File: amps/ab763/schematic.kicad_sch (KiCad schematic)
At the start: 115 parts, among them T1 125P33A, T2 125C3A, T3 125A1A, T4 125A20B

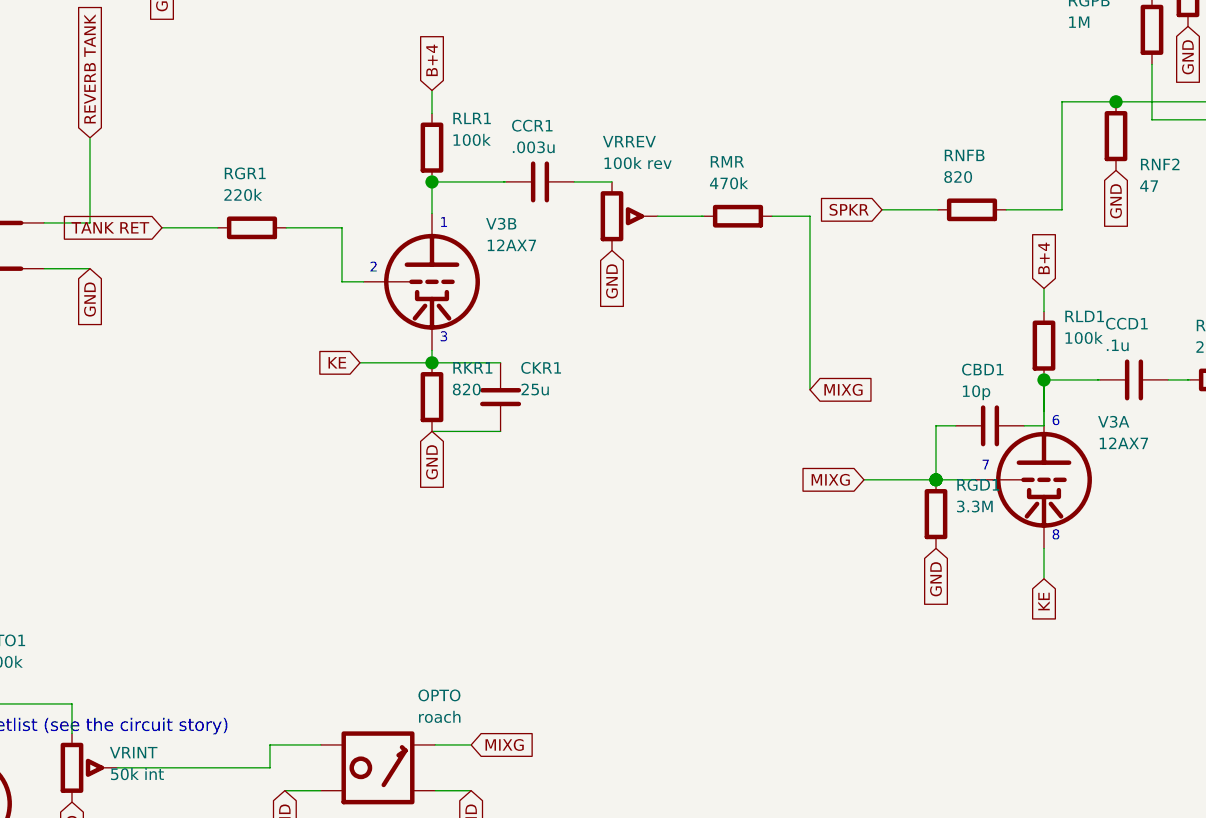
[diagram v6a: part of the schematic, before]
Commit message: Fix: the AB763 mix driver's grid leak was a 3.3M the drawing puts in series, and the reverb return a 220k it puts to ground
The C-FD schematic, read at native size, is VERIFIED on netlist and sheet.
DC operating points are unchanged: GD1 and GR1 sit at 0 V either way, and
verify_amps passes with op-points.yaml as committed.

- Mix-driver grid (node GD1). The drawing's return to ground is a 220k
  (RGD2, new in the parts list, absent until now). The 3.3M (RGD1) with
  its 10 pF (CBD1) sits in SERIES, from the far side of the vibrato
  channel's .02 coupler to the grid, beside the 470k from the Reverb wiper.
  The netlist modelled the 3.3M as the grid leak. The sheet drew it to
  ground, and drew CBD1 from the grid to the plate. Netlist: RGD1 GD1 0
  3.3meg -> RGD2 GD1 0 220k. Sheet: RGD1 || CBD1 from the RVSEND net (the
  .02's far side, which also feeds the reverb send) to the grid; RGD2 from
  the grid to GND.
- Reverb-recovery grid (node GR1). The drawing puts the tank-return plug, a
  220k to ground and the reverb-pedal switch all on the grid node. The layout
  mounts the 220k at the reverb-pedal jack and wires that jack to the
  tank-return jack. The sheet drew RGR1 in SERIES between the tank and the
  grid, and the netlist stood a 1M (RGRV) in for the return. Netlist: RGRV
  GR1 0 1meg -> RGR1 GR1 0 220k. Sheet: TANK RET on the grid, RGR1 from
  the grid to GND.
- bom.yaml: RGD2 added. RGD1, CBD1, RGR1, CCV2 and CRS roles say what
  each part joins.

verify_schematic_nets ab763: PASS (claimed). The board follows in the next
commit.

Co-Authored-By: Claude Opus 5 (1M context) <noreply@anthropic.com>
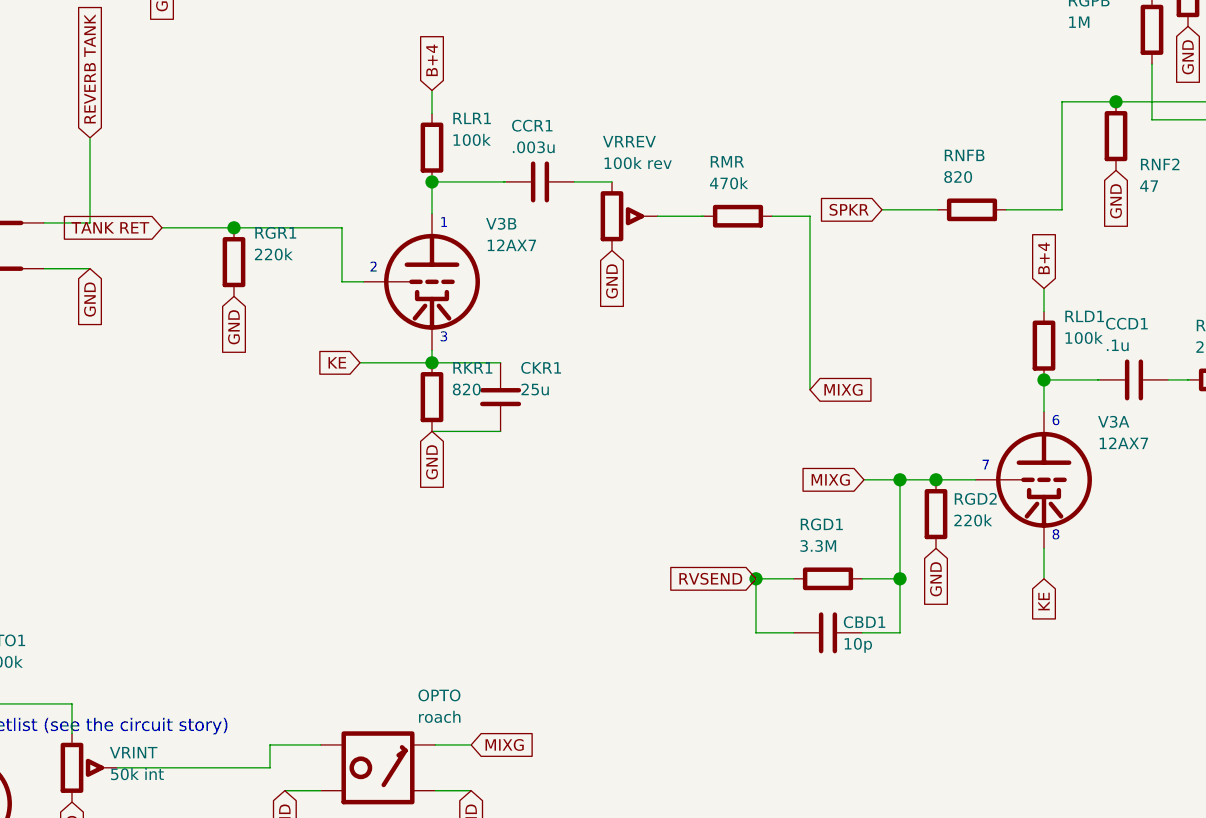
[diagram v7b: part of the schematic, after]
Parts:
- removed CCD1: .1u, symbol cx:C
- removed RD1: 10k, symbol cx:R
- removed RGD1: 3.3M, symbol cx:R
- removed RGL1, RMD1: 220k, symbol cx:R
- removed RT2: 22k, symbol cx:R
- removed RTOG3: 1M, symbol cx:R
- removed V5B: 12AX7, symbol cx:TRIODE
- added C13: 16u, symbol cx:C
- added RGD2: 220k, symbol cx:R
- added RGPB: 1M, symbol cx:R
- added RKTO1: 2.7k, symbol cx:R
- added RTO10: 10M, symbol cx:R
- added V3A, V5A: 12AX7, symbol cx:TRIODE
- added V8: 6V6GT, symbol cx:PENTODE
- added VRSPD: 3M speed, symbol cx:POT
- CCD1: renamed from V5A; value 12AX7 -> .1u; symbol cx:TRIODE -> cx:C
- RD1: renamed from C12; value 16u -> 10k; symbol cx:C -> cx:R
- RGD1: renamed from V3A; value 12AX7 -> 3.3M; symbol cx:TRIODE -> cx:R
- RGL1: renamed from V8; value 6V6GT -> 220k; symbol cx:PENTODE -> cx:R
- RKTO2: renamed from RTO10; value 10M -> 100k
- RT2: renamed from RGPB; value 1M -> 22k
- RTO2: renamed from RKTO2; value 100k -> 220k
- RTOG3: renamed from VRSPD; value 3M speed -> 1M; symbol cx:POT -> cx:R
- V5B: renamed from RKTO1; value 2.7k -> 12AX7; symbol cx:R -> cx:TRIODE
- renumbered C13 to C12, RTO2 to RMD1
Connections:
- net -35V: now also RGL1.2
- net B+2: now also RD1.1
- net B+3: now also C12.1, RD1.2; no longer RD1.1
- net B+4: now also RTO2.1, C13.1; no longer C12.1, RMD1.1
- net GND: now also RGR1.2, RT2.2, RTOG3.2, C13.2, RGD2.2, RKTO1.2, RTO10.2, V8.4 (K), VRSPD.3; no longer RD1.2, RGL1.4 (K), RTO2.2, RTOG3.3, V5B.2
- net KE: now also V3A.3 (K); no longer RGD1.3 (K)
- net MIXG: now also CBD1.2, RGD2.1, V3A.2 (G); no longer CBD1.1
- net PIG: now also RMD1.2
- net RVSEND: now also CBD1.1, RGD1.1
- net TANK RET: now also V3B.2 (G)
- net at RKTO2.1: now also V5B.3 (K); no longer CTO3.2
- net at CPIB.2, V6B.2 (G): now also RGPB.2; no longer RT2.2
- net at C1.2, V7.2 (G1): now also RGL1.1
- net at V5B.1 (P): now also RTO1.2, VRINT.1; no longer CCD1.3 (K)
- net at T3.3 (PRI_B): now also V8.1 (P); no longer RGL1.1 (P)
- net at C2.2, RGL2.1: now also V8.2 (G1); no longer RGL1.2 (G1)
- net at RGPA.2, RT2.1, RTAIL.1: now also RGPB.1
- net at RS2.1: now also V8.3 (G2); no longer RGL1.3 (G2)
- net at CTO2.1, RTOG.1, RTOG3.1: now also V5A.2 (G), VRSPD.1, VRSPD.2 (W); no longer CCD1.2 (G), RTOG3.2 (W)
- net at CTO1.2, CTO3.1: now also RTO2.2, V5A.1 (P); no longer CCD1.1 (P), RMD1.2
- new net: CTO3.2, RTO10.1, V5B.2 (G)
- new net: RKTO1.1, V5A.3 (K)
- new net: CCD1.1, RLD1.2, V3A.1 (P)
- new net: CCD1.2, RMD1.1
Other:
- moved on the sheet: C12, RKTO2, RMD1, RT2, RTO2
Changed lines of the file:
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@@
   (global_label "TANK RET" (shape input) (at 127.7 122.278 180)
     (effects (font (size 1.27 1.27)) (justify right)))
-  (symbol (lib_id "cx:R") (at 137.7 122.278 90) (unit 1)
+  (wire (pts (xy 127.7 122.278) (xy 135.7 122.278))
+    (stroke (width 0) (type default)))
+  (wire (pts (xy 135.7 122.278) (xy 147.7 122.278))
+    (stroke (width 0) (type default)))
+  (junction (at 135.7 122.278) (diameter 1.467) (color 0 0 0 0))
+  (symbol (lib_id "cx:R") (at 135.7 126.088 0) (unit 1)
     (in_bom yes) (on_board yes)
-    (property "Reference" "RGR1" (at 134.5 116.278 270) (effects (font (size 1.27 1.27)) (justify left)))
-    (property "Value" "220k" (at 134.5 118.678 270) (effects (font (size 1.27 1.27)) (justify left))))
-  (wire (pts (xy 127.7 122.278) (xy 133.89 122.278))
-    (stroke (width 0) (type default)))
-  (wire (pts (xy 141.51 122.278) (xy 147.7 122.278))
-    (stroke (width 0) (type default)))
+    (property "Reference" "RGR1" (at 137.9 122.888 0) (effects (font (size 1.27 1.27)) (justify left)))
+    (property "Value" "220k" (at 137.9 125.288 0) (effects (font (size 1.27 1.27)) (justify left))))
+  (global_label "GND" (shape input) (at 135.7 129.898 270)
+    (effects (font (size 1.27 1.27)) (justify right)))
   (wire (pts (xy 147.7 122.278) (xy 147.7 128.278))
     (stroke (width 0) (type default)))
@@
   (global_label "MIXG" (shape input) (at 205.7 150.278 180)
     (effects (font (size 1.27 1.27)) (justify right)))
-  (wire (pts (xy 205.7 150.278) (xy 213.7 150.278))
+  (wire (pts (xy 205.7 150.278) (xy 209.7 150.278))
     (stroke (width 0) (type default)))
+  (wire (pts (xy 209.7 150.278) (xy 213.7 150.278))
+    (stroke (width 0) (type default)))
+  (junction (at 209.7 150.278) (diameter 1.467) (color 0 0 0 0))
   (junction (at 213.7 150.278) (diameter 1.467) (color 0 0 0 0))
   (symbol (lib_id "cx:R") (at 213.7 154.088 0) (unit 1)
     (in_bom yes) (on_board yes)
-    (property "Reference" "RGD1" (at 215.9 150.888 0) (effects (font (size 1.27 1.27)) (justify left)))
-    (property "Value" "3.3M" (at 215.9 153.288 0) (effects (font (size 1.27 1.27)) (justify left))))
+    (property "Reference" "RGD2" (at 215.616 152.448 0) (effects (font (size 1.27 1.27)) (justify left)))
+    (property "Value" "220k" (at 215.616 154.848 0) (effects (font (size 1.27 1.27)) (justify left))))
   (global_label "GND" (shape input) (at 213.7 157.898 270)
     (effects (font (size 1.27 1.27)) (justify right)))
-  (wire (pts (xy 213.7 150.278) (xy 213.7 144.278))
+  (wire (pts (xy 209.7 150.278) (xy 209.7 161.278))
     (stroke (width 0) (type default)))
-  (symbol (lib_id "cx:C") (at 219.7 144.278 90) (unit 1)
+  (wire (pts (xy 209.7 161.278) (xy 209.7 167.278))
+    (stroke (width 0) (type default)))
+  (symbol (lib_id "cx:R") (at 201.7 161.278 90) (unit 1)
     (in_bom yes) (on_board yes)
-    (property "Reference" "CBD1" (at 216.5 138.078 270) (effects (font (size 1.27 1.27)) (justify left)))
-    (property "Value" "10p" (at 216.5 140.478 270) (effects (font (size 1.27 1.27)) (justify left))))
-  (wire (pts (xy 213.7 144.278) (xy 215.89 144.278))
+    (property "Reference" "RGD1" (at 198.5 155.278 270) (effects (font (size 1.27 1.27)) (justify left)))
+    (property "Value" "3.3M" (at 198.5 157.678 270) (effects (font (size 1.27 1.27)) (justify left))))
+  (wire (pts (xy 209.7 161.278) (xy 205.51 161.278))
     (stroke (width 0) (type default)))
-  (wire (pts (xy 223.51 144.278) (xy 225.7 144.278))
+  (wire (pts (xy 197.89 161.278) (xy 193.7 161.278))
     (stroke (width 0) (type default)))
-  (wire (pts (xy 225.7 144.278) (xy 225.7 142.658))
+  (symbol (lib_id "cx:C") (at 201.7 167.278 90) (unit 1)
+    (in_bom yes) (on_board yes)
+    (property "Reference" "CBD1" (at 203.362 166.146 270) (effects (font (size 1.27 1.27)) (justify left)))
+    (property "Value" "10p" (at 203.362 168.546 270) (effects (font (size 1.27 1.27)) (justify left))))
+  (wire (pts (xy 209.7 167.278) (xy 205.51 167.278))
     (stroke (width 0) (type default)))
-  (wire (pts (xy 225.7 142.658) (xy 225.7 139.178))
+  (wire (pts (xy 197.89 167.278) (xy 193.7 167.278))
     (stroke (width 0) (type default)))
+  (wire (pts (xy 193.7 161.278) (xy 193.7 167.278))
+    (stroke (width 0) (type default)))
+  (junction (at 193.7 161.278) (diameter 1.467) (color 0 0 0 0))
+  (junction (at 209.7 161.278) (diameter 1.467) (color 0 0 0 0))
+  (global_label "RVSEND" (shape input) (at 193.7 161.278 180)
+    (effects (font (size 1.27 1.27)) (justify right)))
   (symbol (lib_id "cx:TRIODE") (at 225.7 150.278 0) (unit 1)
     (in_bom yes) (on_board yes)
@@
   (wire (pts (xy 213.7 150.278) (xy 218.08 150.278))
     (stroke (width 0) (type default)))
-  (junction (at 213.7 150.278) (diameter 1.467) (color 0 0 0 0))
   (wire (pts (xy 225.7 142.658) (xy 225.7 139.178))
     (stroke (width 0) (type default)))

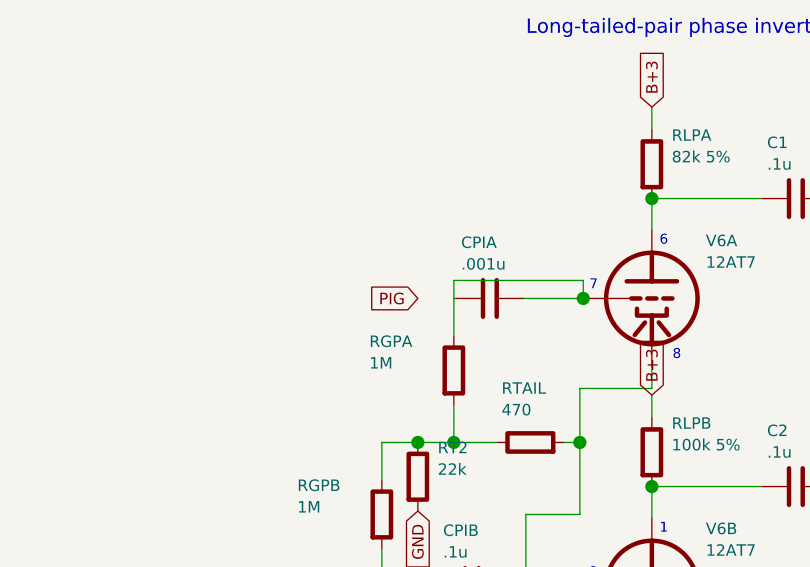
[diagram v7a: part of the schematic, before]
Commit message: Fix: the AB763 sheet's mix node never reached the phase inverter; its .001 coupler sat with both ends on the hot grid
The sheet placed the PI-side PIG label at x=232, but started the lead into
CPIA at x=236, so the label touched nothing. CPIA's left pin also landed on
the RGPA riser (x=236, y=98–104) with a T-tap. The 0.001 µF coupler therefore
sat with both ends on V6A's grid net. The mix node (both channels' 220k
mixing resistors) reached the inverter on no net at all. Neither half is in
the DC netlist, so the sheet↔netlist gate could not see it. It surfaced when
the board placed CPIA as the C-FD layout does, and sheet↔board reported
"the sheet shorts its two ends onto one net".

CPIA now sits left of the RGPA riser, and its lead starts at the label.
CPIA.1 is on {PIG, RMN2, RMD1}; CPIA.2 is on {RGPA, V6A grid}; the riser
crosses the coupler's lead without joining it. A per-anchor scan (every label
anchor must touch a wire, a pin or a junction) now finds none dangling on
this sheet. It finds one MIXG anchor dangling on each of the Super Reverb
and Twin Reverb sheets, which belong to #35.

Co-Authored-By: Claude Opus 5 (1M context) <noreply@anthropic.com>
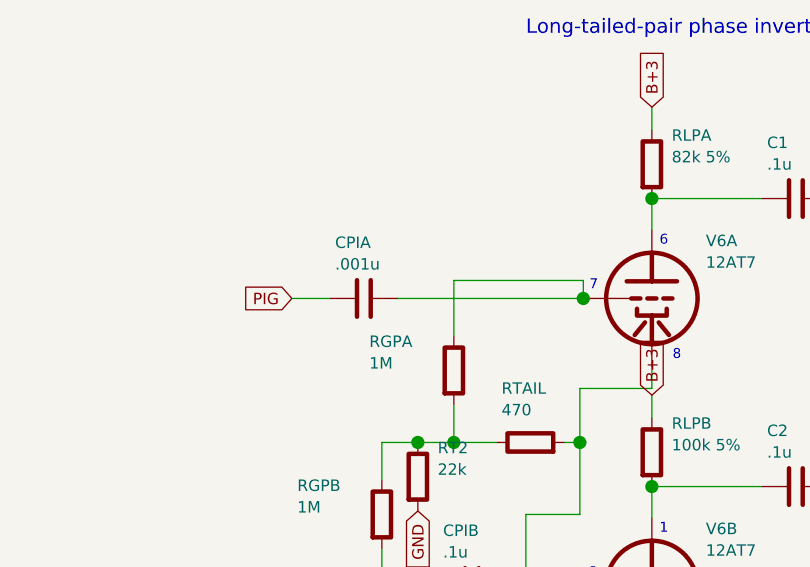
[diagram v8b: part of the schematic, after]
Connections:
- net PIG: now also CPIA.1
- net at CPIA.2, RGPA.1, V6A.2 (G): no longer CPIA.1
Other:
- moved on the sheet: CPIA
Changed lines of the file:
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@@
   (text "Long-tailed-pair phase inverter" (at 253.7 46.278 0)
     (effects (font (size 1.6 1.6)) (justify left)))
-  (global_label "PIG" (shape input) (at 241.7 76.278 180)
+  (global_label "PIG" (shape input) (at 227.7 76.278 180)
     (effects (font (size 1.27 1.27)) (justify right)))
-  (symbol (lib_id "cx:C") (at 249.7 76.278 90) (unit 1)
+  (symbol (lib_id "cx:C") (at 235.7 76.278 90) (unit 1)
     (in_bom yes) (on_board yes)
-    (property "Reference" "CPIA" (at 246.5 70.078 270) (effects (font (size 1.27 1.27)) (justify left)))
-    (property "Value" ".001u" (at 246.5 72.478 270) (effects (font (size 1.27 1.27)) (justify left))))
-  (wire (pts (xy 245.7 76.278) (xy 245.89 76.278))
+    (property "Reference" "CPIA" (at 232.5 70.078 270) (effects (font (size 1.27 1.27)) (justify left)))
+    (property "Value" ".001u" (at 232.5 72.478 270) (effects (font (size 1.27 1.27)) (justify left))))
+  (wire (pts (xy 227.7 76.278) (xy 231.89 76.278))
     (stroke (width 0) (type default)))
-  (wire (pts (xy 253.51 76.278) (xy 260.08 76.278))
+  (wire (pts (xy 239.51 76.278) (xy 260.08 76.278))
     (stroke (width 0) (type default)))
   (symbol (lib_id "cx:TRIODE") (at 267.7 76.278 0) (unit 1)
@@
   (wire (pts (xy 245.7 88.088) (xy 245.7 92.278))
     (stroke (width 0) (type default)))
-  (wire (pts (xy 245.7 80.468) (xy 245.7 76.278))
-    (stroke (width 0) (type default)))
-  (wire (pts (xy 245.7 76.278) (xy 245.7 74.278))
+  (wire (pts (xy 245.7 80.468) (xy 245.7 74.278))
     (stroke (width 0) (type default)))
   (wire (pts (xy 245.7 74.278) (xy 260.08 74.278))
